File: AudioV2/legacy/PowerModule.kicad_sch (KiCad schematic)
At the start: 14 parts, among them J201 +15/-15/A_GND out, J202 PD module in (1=GND 2=+12V), J203 VCC_TONE OUT (1=A_GND 2=9V), U201 REC10K-2415DAW/H2, U202 LM7809 +9V

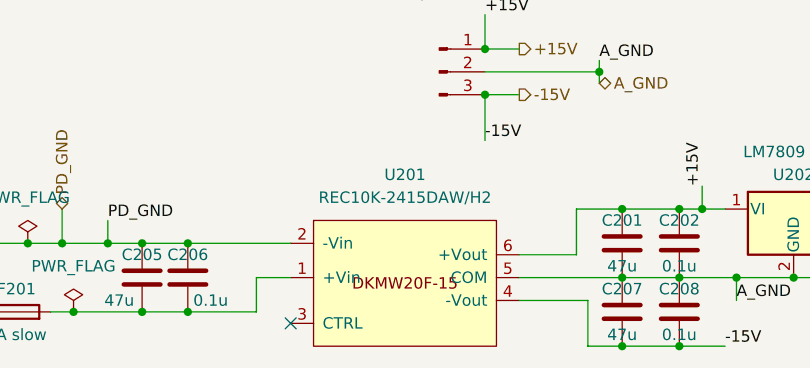
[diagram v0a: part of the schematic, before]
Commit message: AudioV2: REC10K シンボルが DKMW20F-15 を名乗っていたのを直し、A5 を反映
REC10K-2415DAW シンボルは DKMW20F-15 からのコピーで作られ(6cc4b29)、
同定情報が4つとも旧品のままだった。Value / Footprint / Datasheet は
正しかったので気づきにくかった。

  Description   Mean Well DKMW20F-15 ±660mA Cout 650uF → Recom REC10K-2415DAW/H2
  Manufacturer  MEAN WELL                              → RECOM Power
  MPN           DKMW20F-15                             → REC10K-2415DAW/H2
  図形テキスト  DKMW20F-15                             → REC10K-2415DAW

MPN は発注型番なので実害がある。Description は BOM の Role 列に出るため
PARTS.md にもそのまま載っていた。

数値は AGENT_HANDOFF §2.10 のデータシート確認記録から取った
(9-36Vin / ±15V ±333mA 10W / Cout ±270uF / 1.6kVDC / pin3=CTRL open=ON)。
同ファイルの DKMW20F-12 / DKMW20F-15 シンボルは Mean Well 品として
正しいので触っていない。

直した箇所は AudioV2.kicad_sym のシンボル定義と、build_motherboard.py が
素材として読む legacy/PowerModule.kicad_sch の lib_symbols キャッシュ＋
インスタンス。両方直さないと再生成で戻る。

あわせて c9cbb43 が残した「要再生成」を消化した。娘基板スロットの
フットプリント(PinSocket 2x05 / 2x06)が母板側に入った。

検証:
- check_sexpr -q AudioV2  13/0（git 管理下。ローカルには .kicad-mcp の作業
  ファイル2つが増えるが gitignore 済み）
- sch_import --roundtrip  全 OK
- build_motherboard.py を2回回してバイト一致（冪等）
- ERC 29 件・内訳も変化なし
- netlist を再生成前と構造比較: 部品 370 / ネット 327 / ネット名の差なし /
  接続が違うネットなし / 重複参照 0 / 未注釈 0

AudioV2Case.kicad_sch に 207 行の並べ替えが出るのは、f04f0ad で KiCad が
保存した並びとスクリプトが書く並びが違うため。上のネットリスト比較で
内容同一を確認している。

Co-Authored-By: Claude Opus 5 <noreply@anthropic.com>
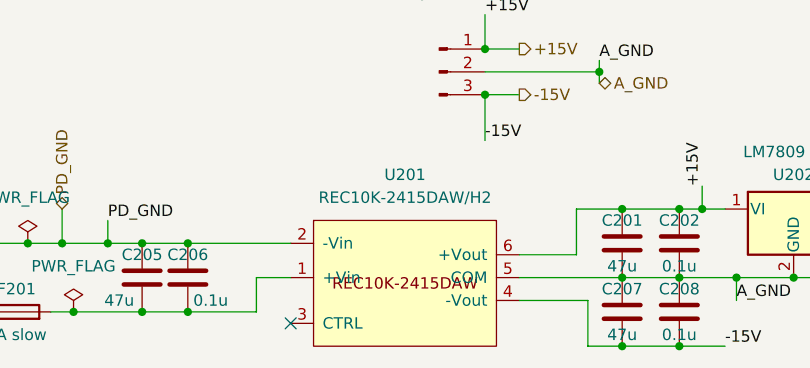
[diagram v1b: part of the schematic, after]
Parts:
- U201: MPN DKMW20F-15 -> REC10K-2415DAW/H2; Manufacturer MEAN WELL -> RECOM Power
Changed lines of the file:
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@@
 			)
 		)
-		(property "Description" "Mean Well DKMW20F-15 isolated DC/DC, 9-36Vin, ±15V/±660mA, DIP 1in x 1in, Cout 650uF/rail; DS datasheets/MeanWell_SKMW20_DKMW20.pdf"
+		(property "Description" "Recom REC10K-2415DAW/H2 isolated DC/DC, 9-36Vin, ±15V/±333mA (10W), 1.6kVDC iso, DIP 1in x 1in, Cout ±270uF/rail, pin3=CTRL open=ON"
 			(at 111.76 76.2 0)
 			(hide yes)
@@
 			)
 		)
-		(property "Manufacturer" "MEAN WELL"
+		(property "Manufacturer" "RECOM Power"
 			(at 111.76 76.2 0)
 			(hide yes)
@@
 			)
 		)
-		(property "MPN" "DKMW20F-15"
+		(property "MPN" "REC10K-2415DAW/H2"
 			(at 111.76 76.2 0)
 			(hide yes)

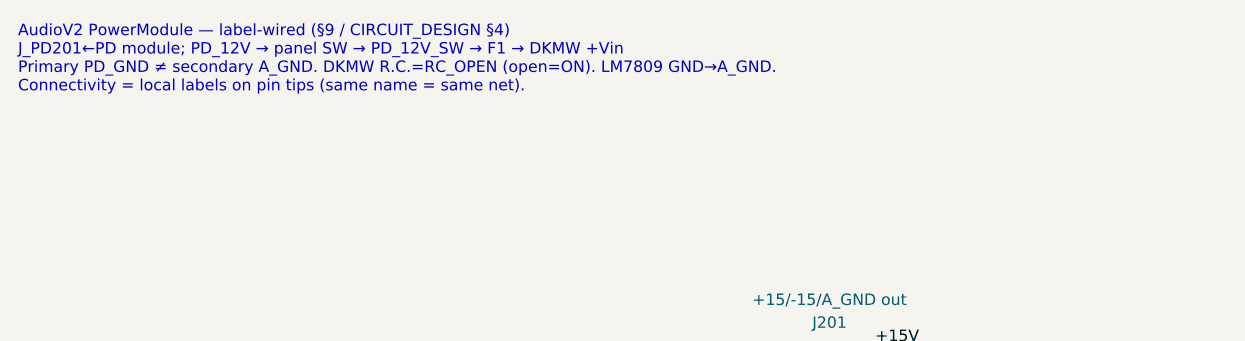
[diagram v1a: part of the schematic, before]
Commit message: AudioV2: NetTie の in_bom を揃え、腐った回路図注記をネット名で書き直した
## NetTie の in_bom（項目1）

NT101（母板）が in_bom=yes、NT1601/NT1602（MeasureControl）が in_bom=no で
不揃いだった。KiCad 標準 Device:NetTie_2 の既定は in_bom=no で、手編集所有の
MeasureControl 側が正しい。NetTie は基板上の銅箔で、買う部品ではない。

NT101 は build_motherboard.py が作っているので生成器側を直した。
symbol_inst_v10 が (in_bom yes) を固定で出していたので引数化した
（既定 True = 従来動作。娘基板スロットなど実在するコネクタは yes のまま）。

in_bom 以外のフラグ（exclude_from_sim / on_board / in_pos_files / dnp）は
NT1601 と一致していたので触っていない。

## 回路図注記（項目2）

PowerModule シートの注記が4つとも腐っていた。designator を書いたせいで
再アノテーションで全滅した、SOURCE_OF_TRUTH が禁じている典型例:

  J_PD201  → 存在しない（現図にその参照は無い）
  F1       → 存在しない
  DKMW     → REC10K-2415DAW/H2 に差し替え済み（2026-09-02）
  RC_OPEN  → **そのネット自体が存在しない**。ネットリストで CTRL ピンは
             unconnected-(U201-CTRL-Pad3) で、素の未接続だった（open=ON なので
             機能は正しい。AGENT_HANDOFF §2.10 の記述どおり）

designator を新しい番号に置き換えても同じことが起きるので、ネット名・機能名
（PD module / panel SW / fuse / DC-DC / PD_12V / PD_12V_SW / PD_GND / A_GND）
で書き直した。素材の legacy/PowerModule.kicad_sch を直して再生成で伝播させた。

## Footprint 未設定（項目3）

44 個が空だった。legacy/ からそのまま持ってきた電源・トーン・出力段・パネル
部品で、生成コードで作った部品には入っている。

**割り当てはしていない。** 物理部品の外形が基板面積を決める設計判断で、
AudioV2 の PCB はまだ設計していない。代わりに見えなくしないための手当:

- 生成ブロックに「Footprint 未設定 N 個」を出す（数値は生成物なので腐らない）
- PARTS.md §5（レイアウト時のバケツ）に項目を追加

## 検証

- check_sexpr -q AudioV2  13/0（git 管理下）
- sch_import --roundtrip   MotherBoard / legacy/PowerModule ともに OK
- ERC 29 件・内訳も変化なし
- netlist 370 / 重複 0 / 未注釈 0（in_bom はネットリストに影響しない）
- netlist に RC_OPEN と DKMW が 0 件であることを確認
- BOM 368 → 367。370-367 = NetTie 3個で、3つの設定が揃った
- gen_parts_bom --check rc=0
- AudioV2Case.kicad_sch は差分ゼロ（build_motherboard.py の決定論性を確認）

## 申し送り

**build_daughter.py は非決定論的で、CLAUDE.md の「冪等・再実行でバイト一致」は
この1本については成立していない。** 2回連続で回すと AmpBankSwitch.kicad_sch が
バイト不一致になる（sch_helpers.new_uid() が uuid4 = 乱数）。今回それに気づいた
ため、娘基板と親は生成し直さずに戻し、母板だけ再生成した。修正は UUID の採り方
の方針決定を伴うので別件。

Co-Authored-By: Claude Opus 5 <noreply@anthropic.com>
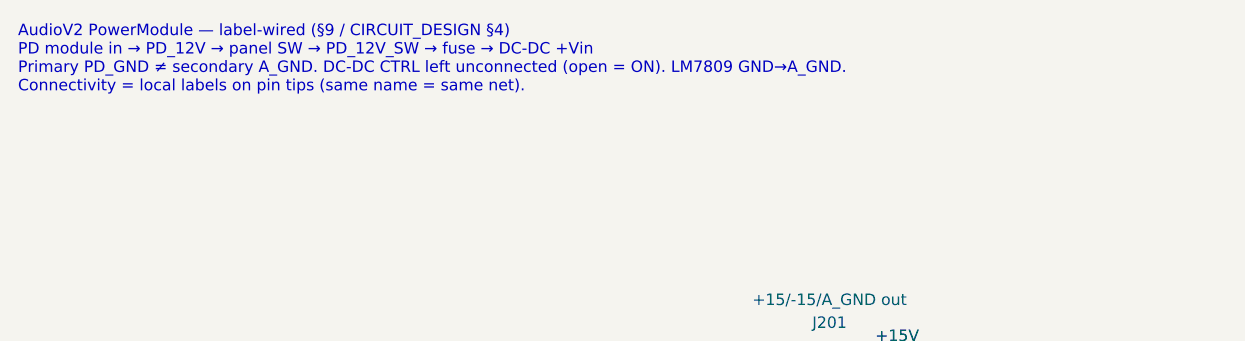
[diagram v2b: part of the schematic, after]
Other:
- note added: "AudioV2 PowerModule — label-wired (§9 / CIRCUIT_DESIGN §4) PD module in → PD_12V → panel SW → PD_12V_SW → fuse → DC-DC +Vin Primary PD_GND ≠ secondary A_GND. DC-DC CTRL left unconnected (open = ON). LM7809 GND→A_GND. Connectivity = local labels on pin tips (same name = same net)."
- note removed: "AudioV2 PowerModule — label-wired (§9 / CIRCUIT_DESIGN §4) J_PD201←PD module; PD_12V → panel SW → PD_12V_SW → F1 → DKMW +Vin Primary PD_GND ≠ secondary A_GND. DKMW R.C.=RC_OPEN (open=ON). LM7809 GND→A_GND. Connectivity = local labels on pin tips (same name = same net)."
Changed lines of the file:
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@@
 	(generator_version "10.0")
 	(paper "A4")
-	(text "AudioV2 PowerModule — label-wired (§9 / CIRCUIT_DESIGN §4)\nJ_PD201←PD module; PD_12V → panel SW → PD_12V_SW → F1 → DKMW +Vin\nPrimary PD_GND ≠ secondary A_GND. DKMW R.C.=RC_OPEN (open=ON). LM7809 GND→A_GND.\nConnectivity = local labels on pin tips (same name = same net)."
+	(text "AudioV2 PowerModule — label-wired (§9 / CIRCUIT_DESIGN §4)\nPD module in → PD_12V → panel SW → PD_12V_SW → fuse → DC-DC +Vin\nPrimary PD_GND ≠ secondary A_GND. DC-DC CTRL left unconnected (open = ON). LM7809 GND→A_GND.\nConnectivity = local labels on pin tips (same name = same net)."
 		(exclude_from_sim no)
 		(at 25.4 20.32 0)

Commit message: AudioV2: +9V LDO の Value を選定品へ揃え、散逸の数字を2箇所直した
## Value が廃番側を名乗っていた

回路図の Value は `LM7809 +9V`、PARTS.md の選定は `ST L7809CV`。TI の `LM78xx` は
廃番系で、ST の `L78xx` は別系列（ユーザー確認: L7809CV は生産中）。**選定自体は
廃番品ではなかった**が、Value が違うものを名乗っていると BOM の Value 列から
廃番側を発注しかねない。今日直した DC-DC の MPN と同じ構図。

Value を `L7809CV +9V` に揃えた。**シンボルは KiCad 標準の
`Regulator_Linear:LM7809_TO220` のまま**で、これは 78xx 共通のピン配置の型
（`LM7805` を extends）。ライブラリ名としての `LM7809_TO220` は netlist にも
残るが、これは正しい。

素材（legacy/PowerModule.kicad_sch）と実図（MotherBoard.kicad_sch）の**両方を
同じ値にした**ので、次の再生成でも同じ結果になる（所有権に反しない）。実図だけ
直すと再生成で戻り、素材だけ直すと BOM に反映されないため。KiCad の正規形式を
崩さずに済むので、差分も5行で収まっている。

## 散逸が2箇所で間違っていた（前提が旧 ±12 V のまま）

入力は +15 V（`U202.1 -> /+15V` をネットリストで確認）。

  PARTS.md         (12-9)×30mA ≈ 0.09 W   ← 12 V 入力前提
  CIRCUIT_DESIGN   ≈0.12 W                ← 13 V 前提?
  正しくは         (15-9)×30mA ≈ 0.18 W   ← 2倍

TO-220 なら放熱器なしで余裕なので実害はないが、数字としては誤り。
入力電圧の出典もその場に書いた。

検証: check_sexpr 13/0、roundtrip OK、ERC 29 件・内訳不変、
netlist 部品 370 / 重複 0 / 未注釈 0、gen_parts_bom で BOM が
`U202 | L7809CV +9V` に更新。

Co-Authored-By: Claude Opus 5 <noreply@anthropic.com>
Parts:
- U202: value LM7809 +9V -> L7809CV +9V
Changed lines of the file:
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@@
 			)
 		)
-		(property "Value" "LM7809 +9V"
+		(property "Value" "L7809CV +9V"
 			(at 154.94 71.12 0)
 			(show_name no)

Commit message: AudioV2: 未使用の VCC_TONE OUT 端子台を削除し、道具の落とし穴2つを記録した
## J203（VCC_TONE OUT 端子台）を削除

PT2314 が別基板（ControlPanel）にいた時代に、+9V とその戻り A_GND を
同じ 2P ケーブルに同梱してループを避けるための端子台だった（§ の
「+9V と戻りを同じ 2P に同梱し、この 2P 以外では戻りを幹線に結ばない」）。

2026-09-03 の統合で PT2314（U402）が母板に載り、+9V とその戻りが板上の
銅箔で完結するので、ケーブルで引き回す前提そのものが消えた。ユーザー確認のうえ削除。

素材（legacy/PowerModule.kicad_sch）を編集して再生成する経路で消した。
文書側（§ の電源チェーン / 端子台一覧 / ループ回避の方針、WIRING.md の
箱配線表）も追随させた。**ループ回避の原則自体は生きている**ので、
「基板外へ電源を出すときは +V と戻りを同じケーブルに同梱する」は残した。

## ⚠ sch_edit.prune() を生成シートに使ってはいけない（実害あり）

最初に MotherBoard.kicad_sch に対して直接 prune を回したところ、
**ラベル 27 個・階層ラベル 13 個が黙って消えた**（階層ラベルはシート界面なので
親子の接続が壊れる）。素材側では同じ操作でワイヤ3本だけだった。

原因: この設計は生成コードの net_at() 方式で**ラベルをピン先に直置き**して
ワイヤに乗せない。prune は「ワイヤに触れていないラベルは浮き」と判定するので、
設計の本体を浮きと誤認する。prune の docstring 自身が過去の過剰削除を
警告していたのに、生成シートに適用してしまった。

push 前に気づいて git checkout で完全復元（階層 24 / ラベル 167 / J203 あり）。
CLAUDE.md と prune() の docstring の両方に警告を書いた。

## ⚠ KiCad 保存後の再生成は2巡回す（実測）

KiCad の正規形式から再生成すると、**1巡目は過渡状態**で親シートに
LINE_L / LINE_R が二重に入り、ERC の label_dangling が 4 → 6 に増える。
2巡目で収束し、以降は何巡してもバイト一致する。CLAUDE.md に書いた。

## 検証（収束後）

- check_sexpr -q AudioV2  13/0
- sch_import --roundtrip  全6ファイル OK
- 母板のラベル数 階層 24 / 通常 167（HEAD と同数＝破壊なし）
- ERC **29 件・内訳も HEAD と完全一致**（1巡目の 31 件から収束）
- netlist を削除前と構造比較: 部品 370 → 369（**消えたのは J203 のみ**）、
  ネット数 327 で変化なし、ネット名の差なし、接続が変わったのは
  /A_GND と /MotherBoard/VCC_TONE の2本だけで、いずれも J203 のピンが
  抜けただけ。VCC_TONE には U202.3 / U402.1 とデカップリングが残っている
- gen_parts_bom --check rc=0。BOM 367 → 366、Footprint 未設定 44 → 43

大きな差分（35k 行）は方法 A（素材を直して再生成）の代償で、KiCad の正規形式から
生成器の形式へ戻ったぶん。内容は上の netlist 比較で担保している。

Co-Authored-By: Claude Opus 5 <noreply@anthropic.com>
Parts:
- removed J203: VCC_TONE OUT (1=A_GND 2=9V), symbol Connector:Conn_01x02_Pin
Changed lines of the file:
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@@
-	(wire
-		(pts
-			(xy 175.26 85.09) (xy 171.45 85.09)
-		)
-		(stroke
-			(width 0)
-			(type default)
-		)
-	)
 	(wire
 		(pts
@@
 	(wire
 		(pts
-			(xy 175.26 81.28) (xy 177.8 81.28)
-		)
-		(stroke
-			(width 0)
-			(type default)
-		)
-	)
-	(wire
-		(pts
 			(xy 53.34 85.09) (xy 57.15 85.09)
 		)
@@
 		(pts
 			(xy 132.08 92.71) (xy 135.89 92.71)
-		)
-		(stroke
-			(width 0)
-			(type default)
-		)
-	)
-	(wire
-		(pts
-			(xy 175.26 85.09) (xy 175.26 81.28)
 		)
 		(stroke
@@
 					(unit 1)
 				)
-			)
-		)
-	)
-	(symbol
-		(lib_id "Connector:Conn_01x02_Pin")
-		(at 182.88 81.28 180)
-		(unit 1)
-		(body_style 1)
-		(exclude_from_sim no)
-		(in_bom yes)
-		(on_board yes)
-		(in_pos_files yes)
-		(dnp no)
-		(property "Reference" "J203"
-			(at 177.8 67.31 0)
-			(show_name no)
-			(do_not_autoplace no)
-			(effects
-				(font
-					(size 1.27 1.27)
-				)
-			)
-		)
-		(property "Value" "VCC_TONE OUT (1=A_GND 2=9V)"
-			(at 179.07 69.85 0)
-			(show_name no)
-			(do_not_autoplace no)
-			(effects
-				(font
-					(size 1.27 1.27)
-				)
-			)
-		)
-		(property "Footprint" ""
-			(at 208.28 167.64 0)
-			(hide yes)
-			(show_name no)
-			(do_not_autoplace no)
-			(effects
-				(font
-					(size 1.27 1.27)
-				)
-			)
-		)
-		(property "Datasheet" ""
-			(at 208.28 167.64 0)
-			(hide yes)
-			(show_name no)
-			(do_not_autoplace no)
-			(effects
-				(font
-					(size 1.27 1.27)
-				)
-			)
-		)
-		(property "Description" ""
-			(at 208.28 167.64 0)
-			(hide yes)
-			(show_name no)
-			(do_not_autoplace no)
-			(effects
-				(font
-					(size 1.27 1.27)
-				)
-			)
-		)
-		(pin "1"
-		)
-		(pin "2"
-		)
-		(instances
-			(project "AudioV2Case"
-				(path "/a1000001-0001-4001-8001-000000000001/a1000002-0002-4002-8002-000000000002"
-					(reference "J203")
-					(unit 1)
-				)

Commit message: AudioV2: 各コンバータ手前のヒューズを確定し、F201 を T1.6A へ
## 確定内容（DECISIONS §8 に導出つきで記録）

各コンバータの入力に個別に入れる（1本の親で束ねない）。

  PD_12V_SW -> U201  (±15V)      0.96 A     ガラス管 T1.6 A（5x20・ホルダ）
  PD_12V_SW -> U1607 (+5V_D)     ~0.25-0.3 A  PPTC I_hold 0.5 A
  PD_12V_SW -> U403  (+5V_COIL)  ~0.16 A ピーク PPTC I_hold 0.35 A
  +15V      -> U202  (+9V)       ~0.03 A    PPTC I_hold 0.1 A

`U403` が一次側へ移った（前コミット）ので、二次側で守るのは `U202` だけになった。

## 主系だけガラス管、他は PPTC

主系はハード開放が要る（PPTC は開放せず遅い）。小系は立ち上げ中にプローブを
当てるので自己復帰品にする — 一発品だとミスのたびに基板から外して交換になる。
PPTC の温度による hold 低下と直列抵抗は、どちらも余裕内であることを確認した。

## T3.15 A を捨てた理由

旧 DKMW20（20 W・一次 ~2 A）で選んだ定格。REC10K（10 W・一次 ~1 A）には3倍で緩い。
PD ポートの供給能力は 12 V/3〜5 A 級なので故障電流もその範囲に収まり、T3.15 A は
その全域で切れない = 実質「保護なし」だった。

## 突入電流は制約にならなかった（前言の訂正を記録に残した）

以前「保護と突入電流のトレードオフ」と書いたが、実物を見たら違った。DC-DC 入力の
容量は C205 47µF + C206 0.1µF だけで、I²t ≈ 0.03 A²s。5x20 スローブローの溶断 I²t は
桁で 5〜15 A²s 級なので2桁以上の余裕がある。

## 回路図側

`F201` の Value を `3A slow` -> `T1.6A slow 5x20`（素材を直して再生成2巡）。

⚠ **3つの PPTC は部品として未追加。** 定格は確定だが挿入は別作業で、素材（legacy/）側と
MeasureControl（手編集所有）に分かれる。DECISIONS §8 と PARTS.md §2.3 の両方に
⚠ として明記した。

検証: check_sexpr 13/0、roundtrip OK、ERC 29 件・内訳不変、
gen_parts_bom --check rc=0（BOM の F201 が T1.6A slow 5x20 へ更新）。

Co-Authored-By: Claude Opus 5 <noreply@anthropic.com>
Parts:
- F201: value 3A slow -> T1.6A slow 5x20
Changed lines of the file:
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@@
 			)
 		)
-		(property "Value" "3A slow"
+		(property "Value" "T1.6A slow 5x20"
 			(at 68.58 91.44 90)
 			(show_name no)

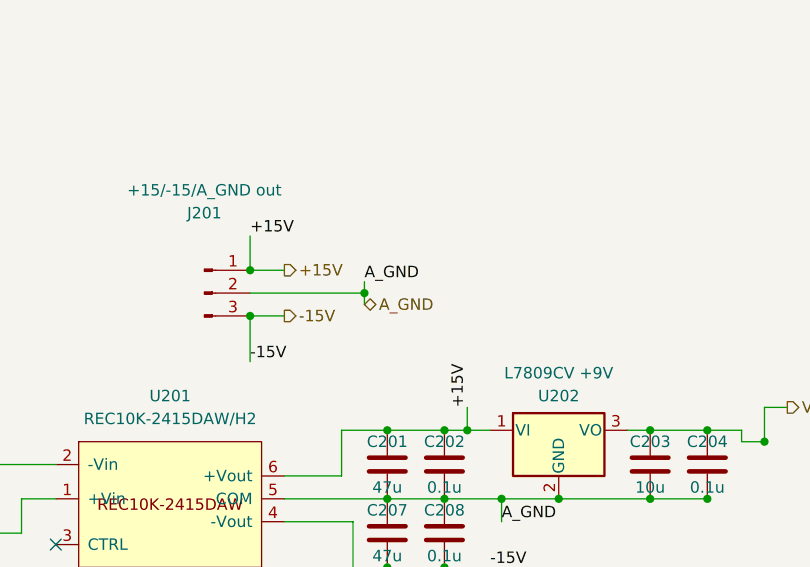
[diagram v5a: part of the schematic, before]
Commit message: AudioV2: PPTC 2個を実装（U403 / U1607 の手前）。U202 は幾何的に入らず未実装
## 実装したもの

  F202  PPTC 0.35A hold  legacy/PowerModule に置き  PD_12V_SW -> PD_12V_COIL -> U403
  F1602 PPTC 0.5A hold   MeasureControl の縦配線を分割 PD_12V_SW -> PD_12V_MEAS -> U1607

F202 は `legacy/ControlPanelAnalog` ではなく `legacy/PowerModule` に置いた。
統合後は同じシートになるのでネットは繋がるうえ、PowerModule には `Device:Fuse` が
既に埋め込まれており lib_symbols の追加が不要。電源保護が電源シートに載るのも筋が通る。
`ControlPanelAnalog` 側は `U403` の入力ラベルを `PD_12V_COIL` へ改名しただけ。

`PD_12V_COIL` / `PD_12V_MEAS` に PWR_FLAG（#FLG0202 / #FLG1602）を追加。
PPTC は受動素子なので、これが無いと KiCad が VIN を「電源が駆動していない」と判定して
ERC が 31 件に増える（実際に増えたので足した）。

## U202 前は未実装（幾何的な理由）

`+15V` の T 点 (144.78,77.47) から `U202.1` (147.32,77.47) への配線が **2.54 mm の
スタブ**で、7.62 mm の素子が入らない。T 点の上流に入れると別の枝も一緒に保護して
しまうので不可。`U202` を数 mm ずらすか引き回しを変える必要があり、それは GUI で
見ながらやる作業。30 mA の枝なので優先度は低い。DECISIONS §8 に⚠として記録した。

## ⚠ 前回の判定を訂正した（DECISIONS の記述も直した）

8c1c558 で「U403 の帰路が二次側へ戻れず通電しない」と書いたが**誤り**。
DECISIONS の A6 が結合チェーンを図示していた:

  A_GND ─NT1601─ ADC_GND ─U1604─ PD_GND ─NT1602─ MC/D_GND
                          (MBC2596 は非絶縁バック。IN- と OUT- は同一ノード)

私の解析は NetTie だけを辿って、この非絶縁バックの内部ボンドを見落としていた。
**帰路は存在した。** 問題は通電の有無ではなく経路で、リレーのパルス電流が結合
チェーン全体、つまり **ADC のアナログ星点を通って**いた。是正の価値は変わらないが、
機構の説明が間違っていたので DECISIONS の D18 実装表を訂正した。

## もう1つ見つけた（未判断）

**`U1604`（`MBC2596-01`、計測系の降圧 DC-DC）はヒューズの外。** `PD_12V_SW` に
直付けで上流は `F1601` のみ。「各コンバータの手前」を徹底するならここにも要る。
DECISIONS §8 に⚠として記録。

## 検証

- check_sexpr 13/0、sch_import --roundtrip 全6ファイル OK
- 再生成は build_daughter -> build_motherboard を2巡（CLAUDE.md の規則）
- **ERC 29 件・内訳も完全一致**（PWR_FLAG 追加前は 31 件）
- 部品 369 -> **371**（F202 / F1602。PWR_FLAG は netlist の components に出ない）
  重複 0 / 未注釈 0
- 結線を netlist で確認:
    /MotherBoard/PD_12V_COIL    = F202.2 + U403.1
    /MeasureControl/PD_12V_MEAS = F1602.2 + U1607.1
    /PD_12V_SW                  = F201.1 / F202.1 / F1602.1 + LED + SW + U1604 + caps
- gen_parts_bom --check rc=0。BOM 366 -> 368

Co-Authored-By: Claude Opus 5 <noreply@anthropic.com>
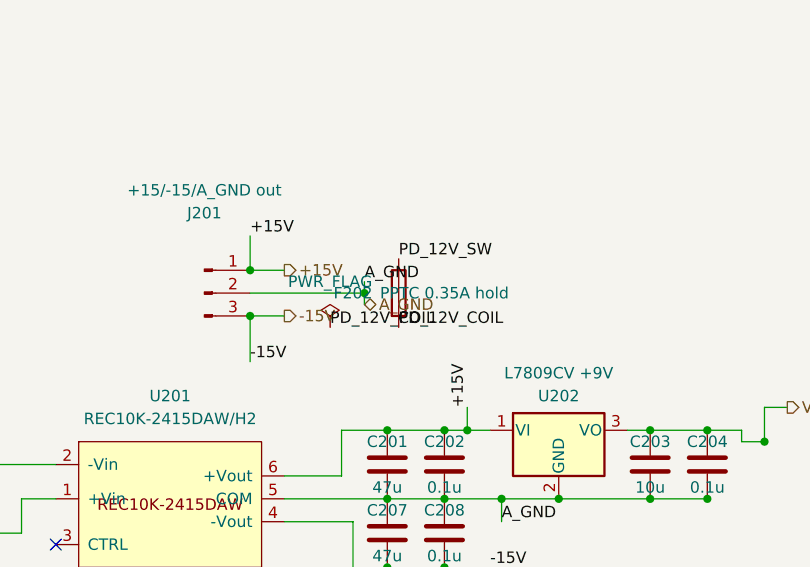
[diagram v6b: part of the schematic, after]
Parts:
- added F202: PPTC 0.35A hold, symbol Device:Fuse
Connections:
- net PD_12V_SW: now also F202.1
- new net PD_12V_COIL: F202.2
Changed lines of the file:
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@@
+		)
+	)
+	(symbol
+		(lib_id "Device:Fuse")
+		(at 137.16 62.23 0)
+		(unit 1)
+		(body_style 1)
+		(exclude_from_sim no)
+		(in_bom yes)
+		(on_board yes)
+		(in_pos_files yes)
+		(dnp no)
+		(property "Reference" "F202"
+			(at 132.07999999999998 62.23 0)
+			(show_name no)
+			(do_not_autoplace no)
+			(effects
+				(font
+					(size 1.27 1.27)
+				)
+			)
+		)
+		(property "Value" "PPTC 0.35A hold"
+			(at 142.24 62.23 0)
+			(show_name no)
+			(do_not_autoplace no)
+			(effects
+				(font
+					(size 1.27 1.27)
+				)
+			)
+		)
+		(property "Footprint" ""
+			(at -12.7 45.72 0)
+			(hide yes)
+			(show_name no)
+			(do_not_autoplace no)
+			(effects
+				(font
+					(size 1.27 1.27)
+				)
+			)
+		)
+		(property "Datasheet" ""
+			(at -12.7 45.72 0)
+			(hide yes)
+			(show_name no)
+			(do_not_autoplace no)
+			(effects
+				(font
+					(size 1.27 1.27)
+				)
+			)
+		)
+		(property "Description" ""
+			(at -12.7 45.72 0)
+			(hide yes)
+			(show_name no)
+			(do_not_autoplace no)
+			(effects
+				(font
+					(size 1.27 1.27)
+				)
+			)
+		)
+		(pin "1"
+		)
+		(pin "2"
+		)
+		(instances
+			(project "AudioV2Case"
+				(path "/a1000001-0001-4001-8001-000000000001/a1000002-0002-4002-8002-000000000002"
+					(reference "F202")
+					(unit 1)
+				)
+			)
+		)
+	)
+	(label "PD_12V_SW"
+		(at 137.16 58.42 0)
+		(effects
+			(font
+				(size 1.27 1.27)
+			)
+			(justify left bottom)
+		)
+	)
+	(label "PD_12V_COIL"
+		(at 137.16 66.04 0)
+		(effects
+			(font
+				(size 1.27 1.27)
+			)
+			(justify left bottom)
+		)
+	)
+	(symbol
+		(lib_id "power:PWR_FLAG")
+		(at 129.54 66.04 0)
+		(unit 1)
+		(body_style 1)
+		(exclude_from_sim no)
+		(in_bom yes)
+		(on_board yes)
+		(in_pos_files yes)
+		(dnp no)
+		(fields_autoplaced yes)
+		(property "Reference" "#FLG0202"
+			(at 129.54 63.5 0)
+			(hide yes)
+			(show_name no)
+			(do_not_autoplace no)
+			(effects
+				(font
+					(size 1.27 1.27)
+				)
+			)
+		)
+		(property "Value" "PWR_FLAG"
+			(at 129.54 60.96 0)
+			(show_name no)
+			(do_not_autoplace no)
+			(effects
+				(font
+					(size 1.27 1.27)
+				)
+			)
+		)
+		(property "Footprint" ""
+			(at 74.93 88.9 0)
+			(hide yes)
+			(show_name no)
+			(do_not_autoplace no)
+			(effects
+				(font
+					(size 1.27 1.27)
+				)
+			)
+		)
+		(property "Datasheet" ""
+			(at 74.93 88.9 0)
+			(hide yes)
+			(show_name no)
+			(do_not_autoplace no)
+			(effects
+				(font
+					(size 1.27 1.27)
+				)
+			)
+		)
+		(property "Description" "Special symbol for telling ERC where power comes from"
+			(at 74.93 88.9 0)
+			(hide yes)
+			(show_name no)
+			(do_not_autoplace no)
+			(effects
+				(font
+					(size 1.27 1.27)
+				)
+			)
+		)
+		(pin "1"
+		)
+		(instances
+			(project "AudioV2Case"
+				(path "/a1000001-0001-4001-8001-000000000001/a1000002-0002-4002-8002-000000000002"
+					(reference "#FLG0202")
+					(unit 1)
+				)
+			)
+		)
+	)
+	(label "PD_12V_COIL"
+		(at 129.54 66.04 0)
+		(effects
+			(font
+				(size 1.27 1.27)
+			)
+			(justify left bottom)
 		)
 	)
